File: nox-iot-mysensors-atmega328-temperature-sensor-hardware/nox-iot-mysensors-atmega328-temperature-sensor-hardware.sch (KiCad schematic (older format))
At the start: 14 parts, among them J1 Vin, J2 FTDI232, J3 AHT10, J4 TP4056, SW1 Reset, U1 ATmega328P-PU, U2 WAVGAT 3.3V, U3 NRF24L01+, Y1 16 MHZ

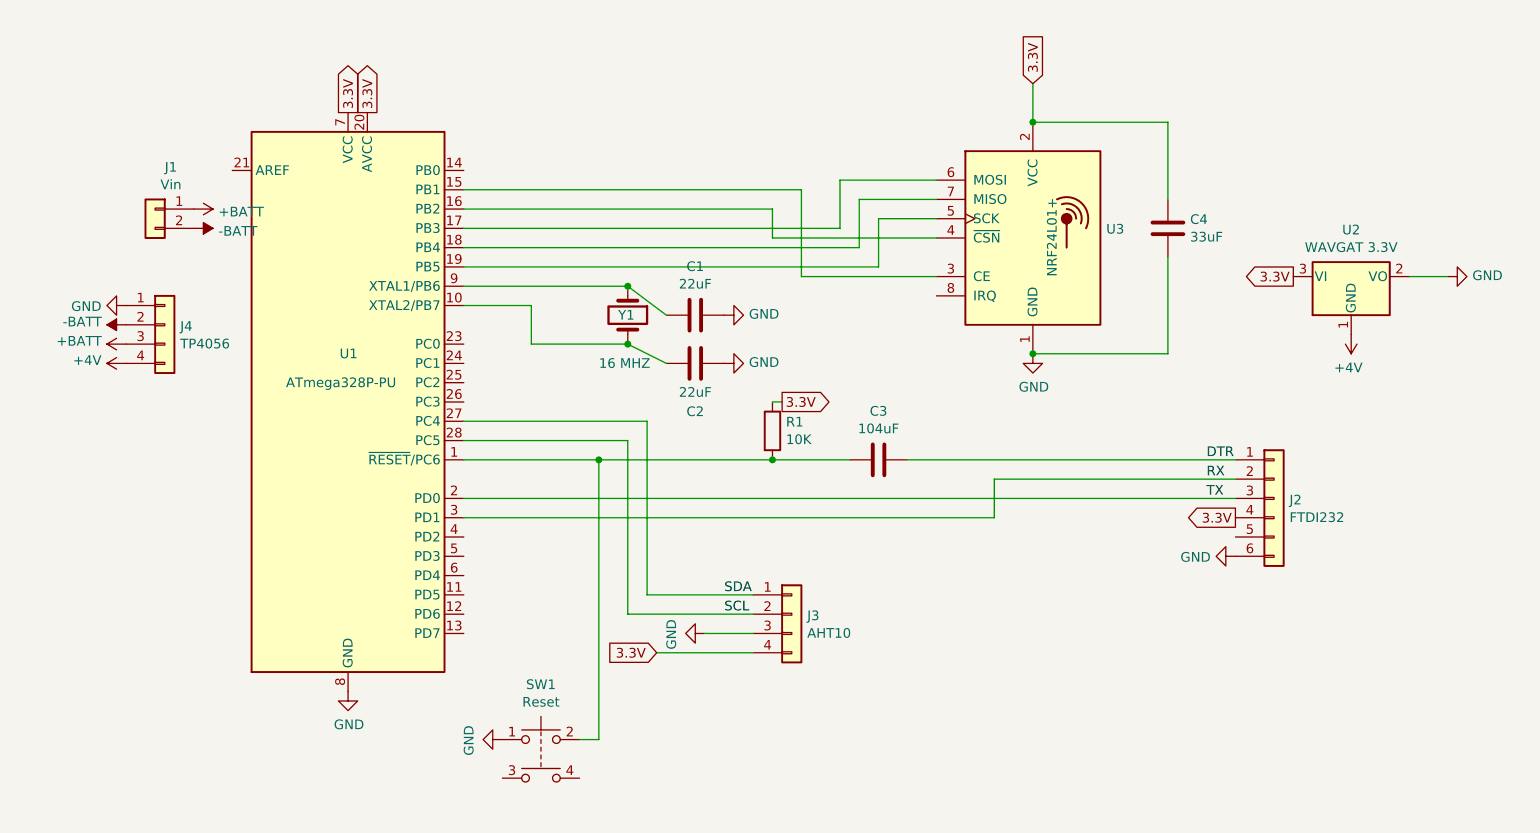
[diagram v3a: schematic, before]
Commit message: adjust to 10uF the NRF24L01 capacitor
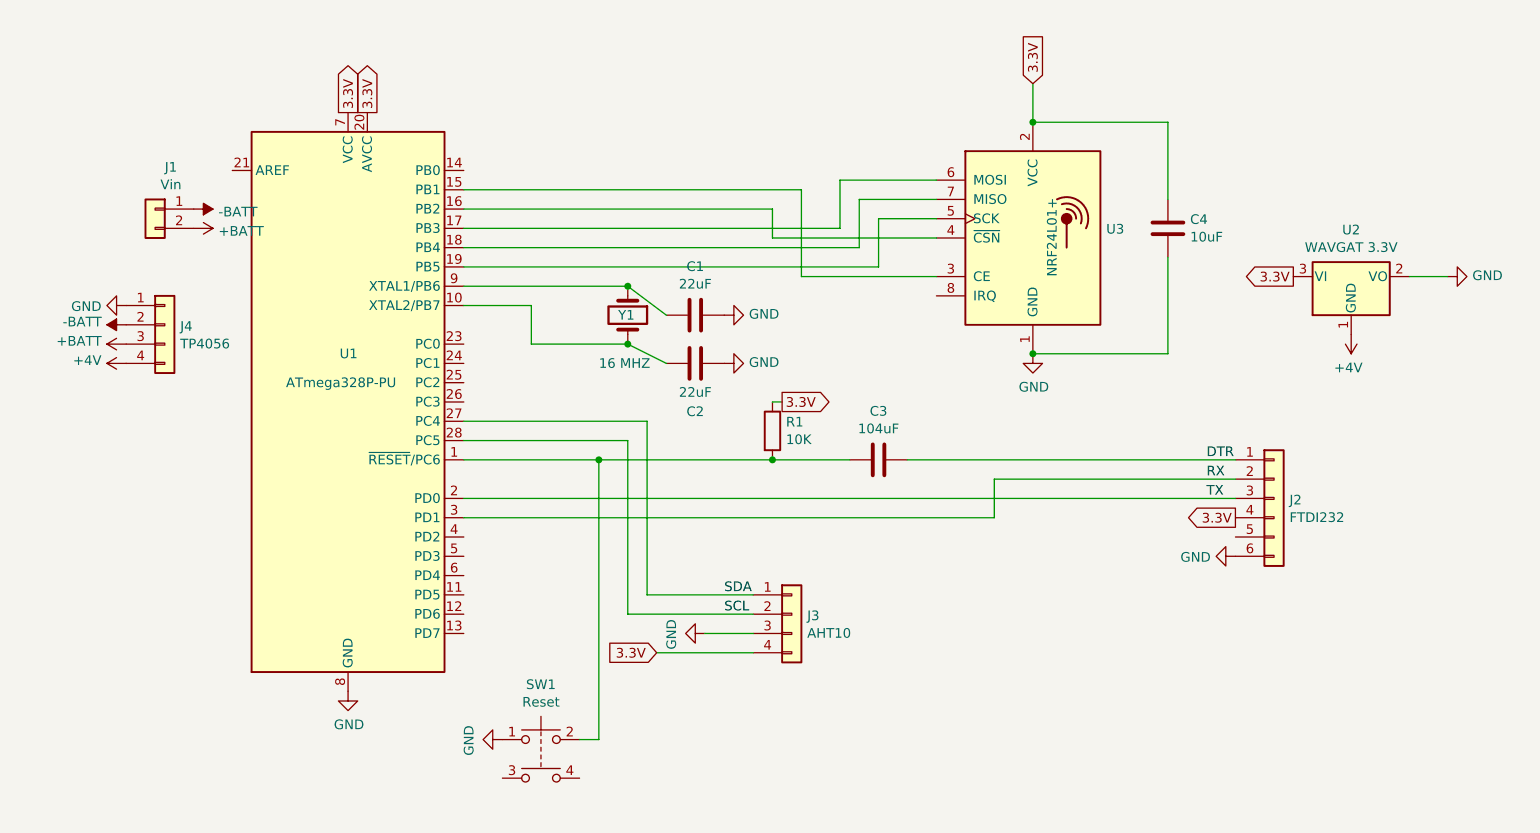
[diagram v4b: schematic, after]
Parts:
- C4: value 33uF -> 10uF; footprint Capacitor_THT:C_Disc_D3.0mm_W1.6mm_P2.50mm -> Capacitor_THT:C_Radial_D6.3mm_H5.0mm_P2.50mm
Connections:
- net +BATT: now also J1.2 (Pin_2); no longer J1.1 (Pin_1)
- net -BATT: now also J1.1 (Pin_1); no longer J1.2 (Pin_2)
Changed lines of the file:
@@
 P 7650 1650
 F 0 "C4" H 7765 1696 50  0000 L CNN
-F 1 "33uF" H 7765 1605 50  0000 L CNN
-F 2 "Capacitor_THT:C_Disc_D3.0mm_W1.6mm_P2.50mm" H 7688 1500 50  0001 C CNN
+F 1 "10uF" H 7765 1605 50  0000 L CNN
+F 2 "Capacitor_THT:C_Radial_D6.3mm_H5.0mm_P2.50mm" H 7688 1500 50  0001 C CNN
 F 3 "~" H 7650 1650 50  0001 C CNN
 	1    7650 1650
@@
 L power:+BATT #PWR0104
 U 1 1 5E783316
-P 2600 1550
-F 0 "#PWR0104" H 2600 1400 50  0001 C CNN
-F 1 "+BATT" V 2615 1678 50  0000 L CNN
-F 2 "" H 2600 1550 50  0001 C CNN
-F 3 "" H 2600 1550 50  0001 C CNN
-	1    2600 1550
+P 2600 1650
+F 0 "#PWR0104" H 2600 1500 50  0001 C CNN
+F 1 "+BATT" V 2615 1778 50  0000 L CNN
+F 2 "" H 2600 1650 50  0001 C CNN
+F 3 "" H 2600 1650 50  0001 C CNN
+	1    2600 1650
 	0    1    1    0
 $EndComp
@@
 L power:-BATT #PWR0109
 U 1 1 5E787B63
-P 2600 1650
-F 0 "#PWR0109" H 2600 1500 50  0001 C CNN
-F 1 "-BATT" V 2615 1778 50  0000 L CNN
-F 2 "" H 2600 1650 50  0001 C CNN
-F 3 "" H 2600 1650 50  0001 C CNN
-	1    2600 1650
-	0    1    1    0
-$EndComp
+P 2600 1550
+F 0 "#PWR0109" H 2600 1400 50  0001 C CNN
+F 1 "-BATT" V 2615 1678 50  0000 L CNN
+F 2 "" H 2600 1550 50  0001 C CNN
+F 3 "" H 2600 1550 50  0001 C CNN
+	1    2600 1550
+	0    1    1    0
+$EndComp

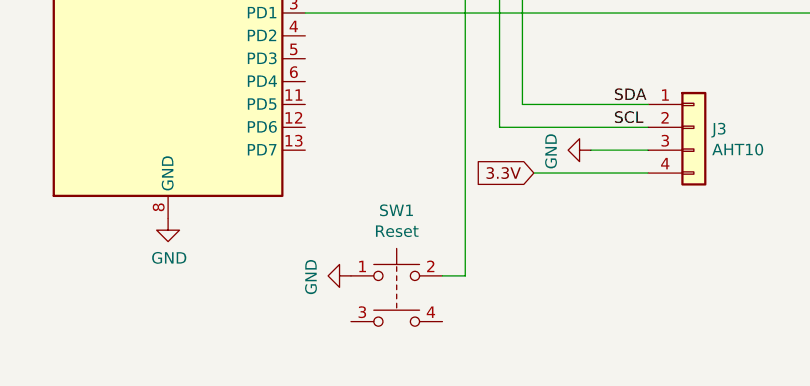
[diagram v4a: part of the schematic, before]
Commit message: change switch button to switch connector
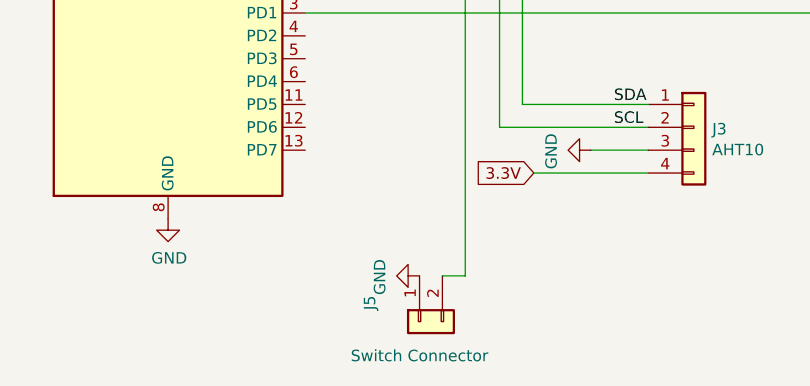
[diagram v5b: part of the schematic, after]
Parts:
- removed SW1: Reset, Button_Switch_THT:SW_TH_Tactile_Omron_B3F-10xx, symbol Switch:SW_Push_Dual
- added J5: Switch Connector, Connector_JST:JST_EH_B2B-EH-A_1x02_P2.50mm_Vertical, symbol Connector_Generic:Conn_01x02
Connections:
- net GND: now also J5.1 (Pin_1)
- net at C3.2, R1.2, U1.1 (~RESET~/PC6): now also J5.2 (Pin_2)
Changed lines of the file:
@@
 	-1   0    0    -1
-$EndComp
-$Comp
-L Switch:SW_Push_Dual SW1
-U 1 1 5E36B497
-P 4400 4300
-F 0 "SW1" H 4400 4585 50  0000 C CNN
-F 1 "Reset" H 4400 4494 50  0000 C CNN
-F 2 "Button_Switch_THT:SW_TH_Tactile_Omron_B3F-10xx" H 4400 4500 50  0001 C CNN
-F 3 "~" H 4400 4500 50  0001 C CNN
-	1    4400 4300
-	1    0    0    -1
-$EndComp
-$Comp
-L power:GND #PWR06
-U 1 1 5E36ED7A
-P 4200 4300
-F 0 "#PWR06" H 4200 4050 50  0001 C CNN
-F 1 "GND" H 4205 4127 50  0000 C CNN
-F 2 "" H 4200 4300 50  0001 C CNN
-F 3 "" H 4200 4300 50  0001 C CNN
-	1    4200 4300
-	0    1    1    0
 $EndComp
 Wire Wire Line
@@
 	0    -1   -1   0
 $EndComp
+$Comp
+L Connector_Generic:Conn_01x02 J5
+U 1 1 5E76E48A
+P 4500 4500
+F 0 "J5" H 4418 4717 50  0000 C CNN
+F 1 "Switch Connector" V 4650 4500 50  0000 C CNN
+F 2 "Connector_JST:JST_EH_B2B-EH-A_1x02_P2.50mm_Vertical" H 4500 4500 50  0001 C CNN
+F 3 "~" H 4500 4500 50  0001 C CNN
+	1    4500 4500
+	0    -1   1    0
+$EndComp
+$Comp
+L power:GND #PWR0111
+U 1 1 5E770C54
+P 4500 4300
+F 0 "#PWR0111" H 4500 4050 50  0001 C CNN
+F 1 "GND" H 4505 4127 50  0000 C CNN
+F 2 "" H 4500 4300 50  0001 C CNN
+F 3 "" H 4500 4300 50  0001 C CNN
+	1    4500 4300
+	0    1    1    0
+$EndComp
 $EndSCHEMATC
